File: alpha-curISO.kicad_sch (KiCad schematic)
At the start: 135 parts, among them SW1 SW_Push_45deg, SW10 SW_Push_45deg, SW11 SW_Push_45deg, SW11(2) SW_Push_45deg, SW12 SW_Push_45deg, SW13 SW_Push_45deg, SW14 SW_Push_45deg, SW15 SW_Push_45deg, SW16 SW_Push_45deg, SW17 SW_Push_45deg, SW18 SW_Push_45deg, SW19 SW_Push_45deg, SW2 SW_Push_45deg, SW20 SW_Push_45deg, SW21 SW_Push_45deg, SW22 SW_Push_45deg, SW22(1.5) SW_Push_45deg, SW23 SW_Push_45deg, SW23(1.5) SW_Push_45deg, SW24 SW_Push_45deg, SW24(2) SW_Push_45deg, SW24(ISO) SW_Push_45deg, SW25(1.25) SW_Push_45deg, SW25(1.5) SW_Push_45deg, SW25(ortho) SW_Push_45deg, SW26 SW_Push_45deg, SW26(ortho) SW_Push_45deg, SW27 SW_Push_45deg, SW27(ortho) SW_Push_45deg, SW28 SW_Push_45deg, SW28(ortho) SW_Push_45deg, SW29 SW_Push_45deg, SW29(ortho) SW_Push_45deg, SW3 SW_Push_45deg, SW30 SW_Push_45deg, SW30(ortho) SW_Push_45deg, SW31 SW_Push_45deg, SW31(ortho) SW_Push_45deg, SW32 SW_Push_45deg, SW32(ortho) SW_Push_45deg, SW33 SW_Push_45deg, SW33(ortho) SW_Push_45deg, SW34 SW_Push_45deg, SW34(ortho) SW_Push_45deg, SW35 SW_Push_45deg, SW35(ortho) SW_Push_45deg, SW36(1.25) SW_Push_45deg, SW36(1.5) SW_Push_45deg, SW36(ortho) SW_Push_45deg, SW37 SW_Push_45deg, SW37(1.5) SW_Push_45deg, SW38 SW_Push_45deg, SW38(3) SW_Push_45deg, SW39 SW_Push_45deg, SW39(1.5) SW_Push_45deg, SW4 SW_Push_45deg, SW40(1.25) SW_Push_45deg, SW40(1.5) SW_Push_45deg, SW40(3) SW_Push_45deg, SW41(1.75) SW_Push_45deg, SW41(1.75a) SW_Push_45deg, SW41(2) SW_Push_45deg, SW41(2.25) SW_Push_45deg, SW42 SW_Push_45deg, SW42(3) SW_Push_45deg, SW42(6) SW_Push_45deg, SW43(1.75) SW_Push_45deg, SW43(2) SW_Push_45deg, SW43(2.25) SW_Push_45deg, SW44(1.25) SW_Push_45deg, SW44(1.5) SW_Push_45deg, SW44(3) SW_Push_45deg, SW45 SW_Push_45deg, SW45(1.5) SW_Push_45deg, SW46 SW_Push_45deg, SW46(3) SW_Push_45deg, SW47 SW_Push_45deg, SW47(1.5) SW_Push_45deg, SW48 SW_Push_45deg, SW49 SW_Push_45deg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

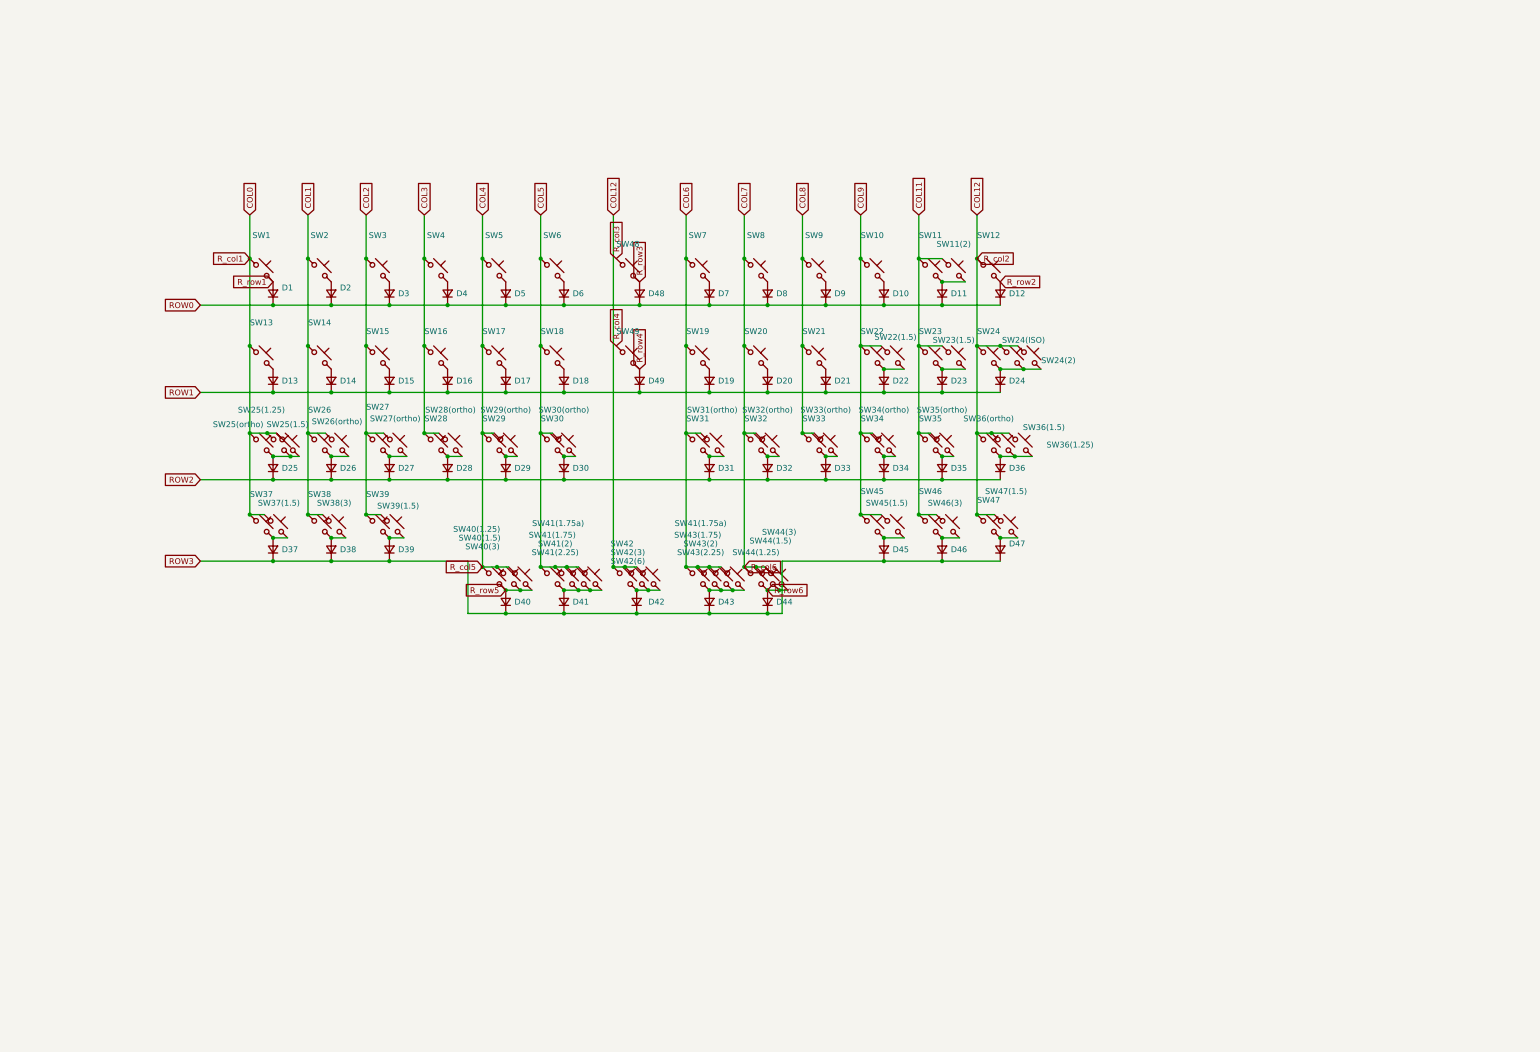
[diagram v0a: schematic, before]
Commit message: add components to schematic
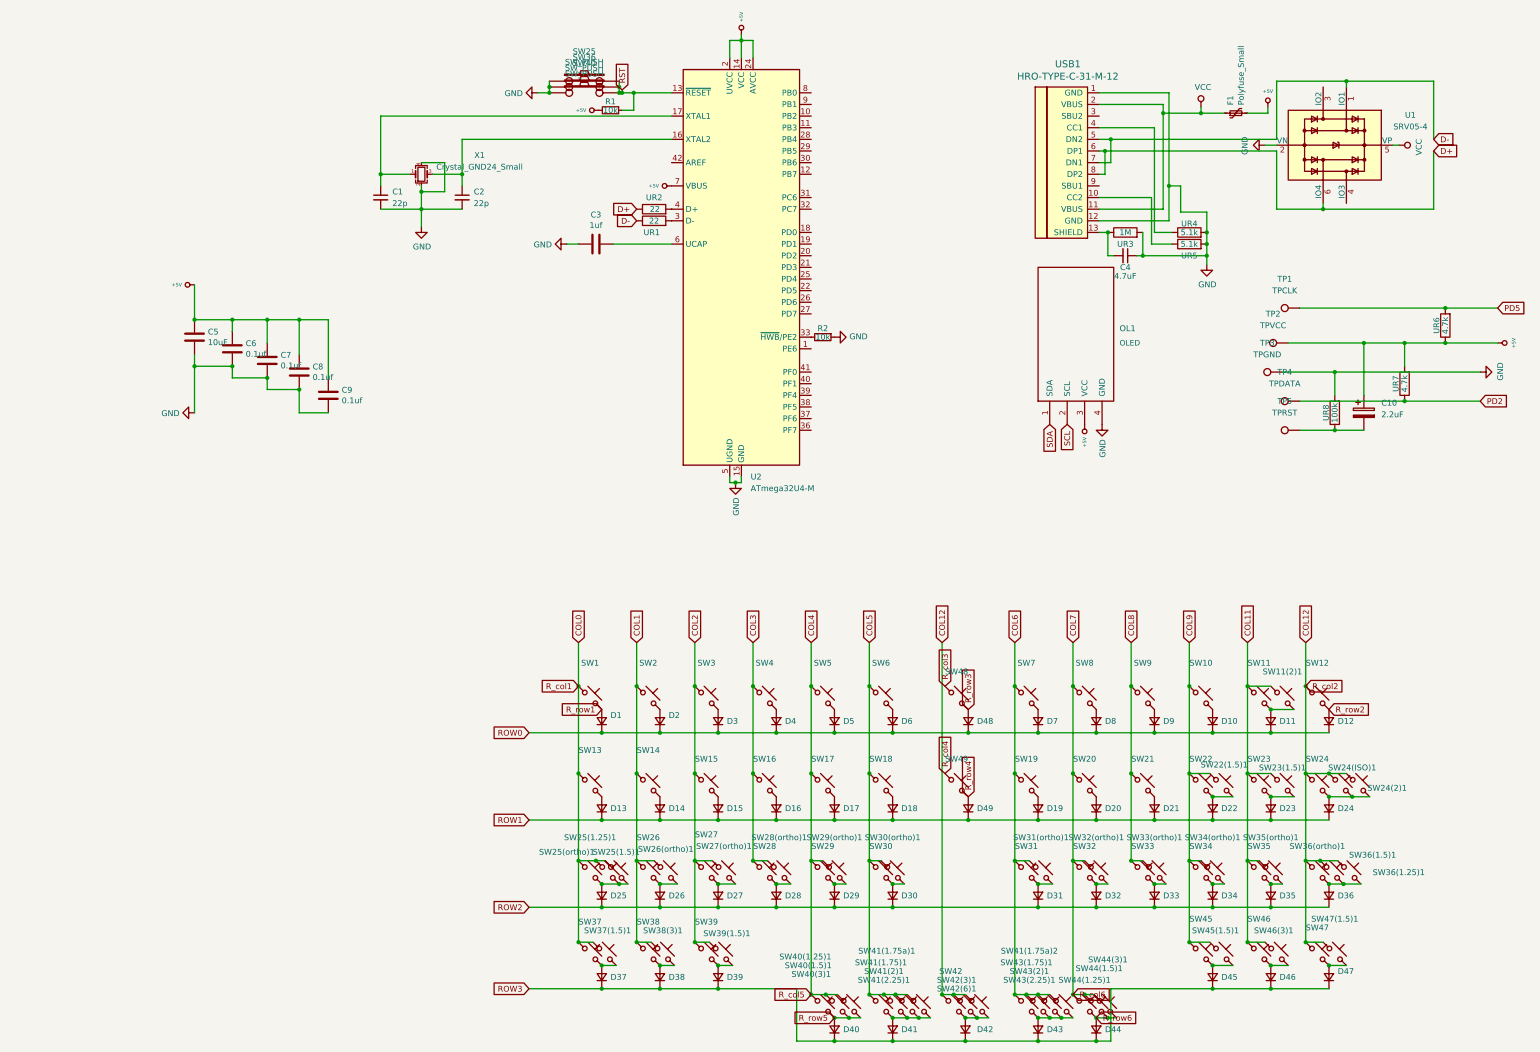
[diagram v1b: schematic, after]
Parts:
- added C1, C2: 22p, Capacitor_SMD:C_0805_2012Metric, symbol Device:C_Small
- added C10: 2.2uF, Capacitor_SMD:C_0805_2012Metric_Pad1.18x1.45mm_HandSolder, symbol Device:C_Polarized
- added C3: 1uf, Capacitor_SMD:C_0805_2012Metric, symbol device:C
- added C4: 4.7uF, Capacitor_SMD:C_0805_2012Metric, symbol device:C_Small
- added C5: 10uF, Capacitor_SMD:C_0805_2012Metric, symbol device:C
- added C6, C7, C8, C9: 0.1uf, Capacitor_SMD:C_0805_2012Metric, symbol device:C
- added F1: Polyfuse_Small, Fuse:Fuse_1206_3216Metric_Pad1.42x1.75mm_HandSolder, symbol device:Polyfuse_Small
- added OL1: OLED, kbd:OLED_v2, symbol kbd:OLED
- added R1, R2: 10k, Resistor_SMD:R_0805_2012Metric, symbol device:R_Small
- added SW25, SW40: SW_PUSH, Button_Switch_SMD:SW_SPST_SKQG_WithoutStem, symbol keyboard_parts:SW_PUSH
- added SW36: SW_PUSH, Connector_PinHeader_2.54mm:PinHeader_1x02_P2.54mm_Vertical, symbol keyboard_parts:SW_PUSH
- added TP1: TPCLK, TestPoint:TestPoint_THTPad_1.0x1.0mm_Drill0.5mm, symbol Connector:TestPoint
- added TP2: TPVCC, TestPoint:TestPoint_THTPad_1.0x1.0mm_Drill0.5mm, symbol Connector:TestPoint
- added TP3: TPGND, TestPoint:TestPoint_THTPad_1.0x1.0mm_Drill0.5mm, symbol Connector:TestPoint
- added TP4: TPDATA, TestPoint:TestPoint_THTPad_1.0x1.0mm_Drill0.5mm, symbol Connector:TestPoint
- added TP5: TPRST, TestPoint:TestPoint_THTPad_1.0x1.0mm_Drill0.5mm, symbol Connector:TestPoint
- added U1: SRV05-4, Package_TO_SOT_SMD:SOT-23-6, symbol Power_Protection:SRV05-4
- added U2: ATmega32U4-M, Package_DFN_QFN:QFN-44-1EP_7x7mm_P0.5mm_EP5.2x5.2mm_ThermalVias, symbol MCU_Microchip_ATmega:ATmega32U4-M
- added UR1, UR2: 22, Resistor_SMD:R_0805_2012Metric, symbol device:R
- added UR3: 1M, Resistor_SMD:R_0805_2012Metric, symbol device:R
- added UR4, UR5: 5.1k, Resistor_SMD:R_0805_2012Metric, symbol device:R
- added UR6, UR7: 4.7k, Resistor_SMD:R_0805_2012Metric_Pad1.20x1.40mm_HandSolder, symbol device:R
- added UR8: 100k, Resistor_SMD:R_0805_2012Metric_Pad1.20x1.40mm_HandSolder, symbol device:R
- added USB1: HRO-TYPE-C-31-M-12, Type-C:HRO-TYPE-C-31-M-12-HandSoldering, symbol Type-C:HRO-TYPE-C-31-M-12
- added X1: Crystal_GND24_Small, Crystal:Crystal_SMD_3225-4Pin_3.2x2.5mm_HandSoldering, symbol Device:Crystal_GND24_Small
- renumbered SW11(2) to SW11(2)1, SW22(1.5) to SW22(1.5)1, SW23(1.5) to SW23(1.5)1, SW24(2) to SW24(2)1, SW24(ISO) to SW24(ISO)1, SW25(1.25) to SW25(1.25)1, SW25(1.5) to SW25(1.5)1, SW25(ortho) to SW25(ortho)1, SW26(ortho) to SW26(ortho)1, SW27(ortho) to SW27(ortho)1, SW28(ortho) to SW28(ortho)1, SW29(ortho) to SW29(ortho)1, SW30(ortho) to SW30(ortho)1, SW31(ortho) to SW31(ortho)1, SW32(ortho) to SW32(ortho)1, SW33(ortho) to SW33(ortho)1, SW34(ortho) to SW34(ortho)1, SW35(ortho) to SW35(ortho)1, SW36(1.25) to SW36(1.25)1, SW36(1.5) to SW36(1.5)1, SW36(ortho) to SW36(ortho)1, SW37(1.5) to SW37(1.5)1, SW38(3) to SW38(3)1, SW39(1.5) to SW39(1.5)1, SW40(1.25) to SW40(1.25)1, SW40(1.5) to SW40(1.5)1, SW40(3) to SW40(3)1, SW41(1.75) to SW41(1.75)1, SW41(1.75a) to SW41(1.75a)1, SW41(1.75a) to SW41(1.75a)2, SW41(2) to SW41(2)1, SW41(2.25) to SW41(2.25)1, SW42(3) to SW42(3)1, SW42(6) to SW42(6)1, SW43(1.75) to SW43(1.75)1, SW43(2) to SW43(2)1, SW43(2.25) to SW43(2.25)1, SW44(1.25) to SW44(1.25)1, SW44(1.5) to SW44(1.5)1, SW44(3) to SW44(3)1, SW45(1.5) to SW45(1.5)1, SW46(3) to SW46(3)1, SW47(1.5) to SW47(1.5)1
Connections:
- new net: U2.3 (D-), UR2.2
- new net: C1.1, U2.17 (XTAL1), X1.1
- new net: C2.1, U2.16 (XTAL2), X1.3
- new net: UR5.1, USB1.10 (CC2)
- new net: C10.2, TP5.1, UR8.1
- new net: UR4.1, USB1.4 (CC1)
- new net: C4.2, UR3.1, USB1.13 (SHIELD)
- new net: U2.4 (D+), UR1.2
- new net: C3.1, U2.6 (UCAP)
- new net: R2.2, U2.33 (~{HWB}/PE2)
- new net +5V: C10.1, C5.1, C6.1, C7.1, C8.1, C9.1, F1.2, OL1.3 (VCC), R1.2, TP2.1, U2.14 (VCC), U2.2 (UVCC), U2.24 (AVCC), U2.34 (VCC), U2.44 (AVCC), U2.7 (VBUS), UR6.1, UR7.2
- new net D+: U1.6 (IO4), UR1.1, USB1.6 (DP1), USB1.8 (DP2)
- new net D-: U1.1 (IO1), UR2.1, USB1.5 (DN2), USB1.7 (DN1)
- new net GND: C1.2, C2.2, C3.2, C4.1, C5.2, C6.2, C7.2, C8.2, C9.2, OL1.4 (GND), R2.1, SW25.1, SW36.1, SW40.1, TP3.1, U1.2 (VN), U2.15 (GND), U2.23 (GND), U2.35 (GND), U2.43 (GND), U2.45 (GND), U2.5 (UGND), UR3.2, UR4.2, UR5.2, UR8.2, USB1.1 (GND), USB1.12 (GND), X1.2, X1.4
- new net PD2: TP4.1, UR7.1
- new net PD5: TP1.1, UR6.2
- new net RST: R1.1, SW25.2, SW36.2, SW40.2, U2.13 (~{RESET})
- new net SCL: OL1.2 (SCL)
- new net SDA: OL1.1 (SDA)
- new net VCC: F1.1, U1.5 (VP), USB1.11 (VBUS), USB1.2 (VBUS)
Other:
- moved on the sheet: D1, D10, D11, D12, D13, D14, D15, D16, D17, D18, D19, D2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

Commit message: split schematics
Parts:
- removed C1, C2: 22p, Capacitor_SMD:C_0805_2012Metric, symbol Device:C_Small
- removed C10: 2.2uF, Capacitor_SMD:C_0805_2012Metric_Pad1.18x1.45mm_HandSolder, symbol Device:C_Polarized
- removed C4: 4.7uF, Capacitor_SMD:C_0805_2012Metric, symbol device:C_Small
- removed C5: 10uF, Capacitor_SMD:C_0805_2012Metric, symbol device:C
- removed C6, C7, C8, C9: 0.1uf, Capacitor_SMD:C_0805_2012Metric, symbol device:C
- removed D1, D10, D11, D12, D13, D14, D15, D16, D17, D18, D19, D2, D20, D21, D22, D23, D24, D25, D26, D27, D28, D29, D3, D30, D31, D32, D33, D34, D35, D36, D37, D38, D39, D4, D40, D41, D42, D43, D44, D45, D46, D47, D48, D49, D5, D6, D7, D8, D9: D_Small, symbol Device:D_Small
- removed F1: Polyfuse_Small, Fuse:Fuse_1206_3216Metric_Pad1.42x1.75mm_HandSolder, symbol device:Polyfuse_Small
- removed OL1: OLED, kbd:OLED_v2, symbol kbd:OLED
- removed R1: 10k, Resistor_SMD:R_0805_2012Metric, symbol device:R_Small
- removed SW1, SW10, SW11, SW11(2)1, SW12, SW13, SW14, SW15, SW16, SW17, SW18, SW19, SW2, SW20, SW21, SW22, SW22(1.5)1, SW23, SW23(1.5)1, SW24, SW24(2)1, SW24(ISO)1, SW25(1.25)1, SW25(1.5)1, SW25(ortho)1, SW26, SW26(ortho)1, SW27, SW27(ortho)1, SW28, SW28(ortho)1, SW29, SW29(ortho)1, SW3, SW30, SW30(ortho)1, SW31, SW31(ortho)1, SW32, SW32(ortho)1, SW33, SW33(ortho)1, SW34, SW34(ortho)1, SW35, SW35(ortho)1, SW36(1.25)1, SW36(1.5)1, SW36(ortho)1, SW37, SW37(1.5)1, SW38, SW38(3)1, SW39, SW39(1.5)1, SW4, SW40(1.25)1, SW40(1.5)1, SW40(3)1, SW41(1.75)1, SW41(1.75a)1, SW41(1.75a)2, SW41(2)1, SW41(2.25)1, SW42, SW42(3)1, SW42(6)1, SW43(1.75)1, SW43(2)1, SW43(2.25)1, SW44(1.25)1, SW44(1.5)1, SW44(3)1, SW45, SW45(1.5)1, SW46, SW46(3)1, SW47, SW47(1.5)1, SW48, SW49, SW5, SW6, SW7, SW8, SW9: SW_Push_45deg, symbol Switch:SW_Push_45deg
- removed SW25, SW40: SW_PUSH, Button_Switch_SMD:SW_SPST_SKQG_WithoutStem, symbol keyboard_parts:SW_PUSH
- removed SW36: SW_PUSH, Connector_PinHeader_2.54mm:PinHeader_1x02_P2.54mm_Vertical, symbol keyboard_parts:SW_PUSH
- removed TP1: TPCLK, TestPoint:TestPoint_THTPad_1.0x1.0mm_Drill0.5mm, symbol Connector:TestPoint
- removed TP2: TPVCC, TestPoint:TestPoint_THTPad_1.0x1.0mm_Drill0.5mm, symbol Connector:TestPoint
- removed TP3: TPGND, TestPoint:TestPoint_THTPad_1.0x1.0mm_Drill0.5mm, symbol Connector:TestPoint
- removed TP4: TPDATA, TestPoint:TestPoint_THTPad_1.0x1.0mm_Drill0.5mm, symbol Connector:TestPoint
- removed TP5: TPRST, TestPoint:TestPoint_THTPad_1.0x1.0mm_Drill0.5mm, symbol Connector:TestPoint
- removed U1: SRV05-4, Package_TO_SOT_SMD:SOT-23-6, symbol Power_Protection:SRV05-4
- removed UR3: 1M, Resistor_SMD:R_0805_2012Metric, symbol device:R
- removed UR4, UR5: 5.1k, Resistor_SMD:R_0805_2012Metric, symbol device:R
- removed UR6, UR7: 4.7k, Resistor_SMD:R_0805_2012Metric_Pad1.20x1.40mm_HandSolder, symbol device:R
- removed UR8: 100k, Resistor_SMD:R_0805_2012Metric_Pad1.20x1.40mm_HandSolder, symbol device:R
- removed USB1: HRO-TYPE-C-31-M-12, Type-C:HRO-TYPE-C-31-M-12-HandSoldering, symbol Type-C:HRO-TYPE-C-31-M-12
- removed X1: Crystal_GND24_Small, Crystal:Crystal_SMD_3225-4Pin_3.2x2.5mm_HandSoldering, symbol Device:Crystal_GND24_Small
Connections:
- net XTAL1: now reaches U2.17 (XTAL1)
- net XTAL2: now reaches U2.16 (XTAL2)
- no-connect marks 0 -> 1
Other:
- added sheet Components (Components.kicad_sch)
- added sheet Switch Matrix (Switch Matrix.kicad_sch)
- moved on the sheet: C3, R2, U2, UR1, UR2
